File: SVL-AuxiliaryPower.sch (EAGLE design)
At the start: 24 parts

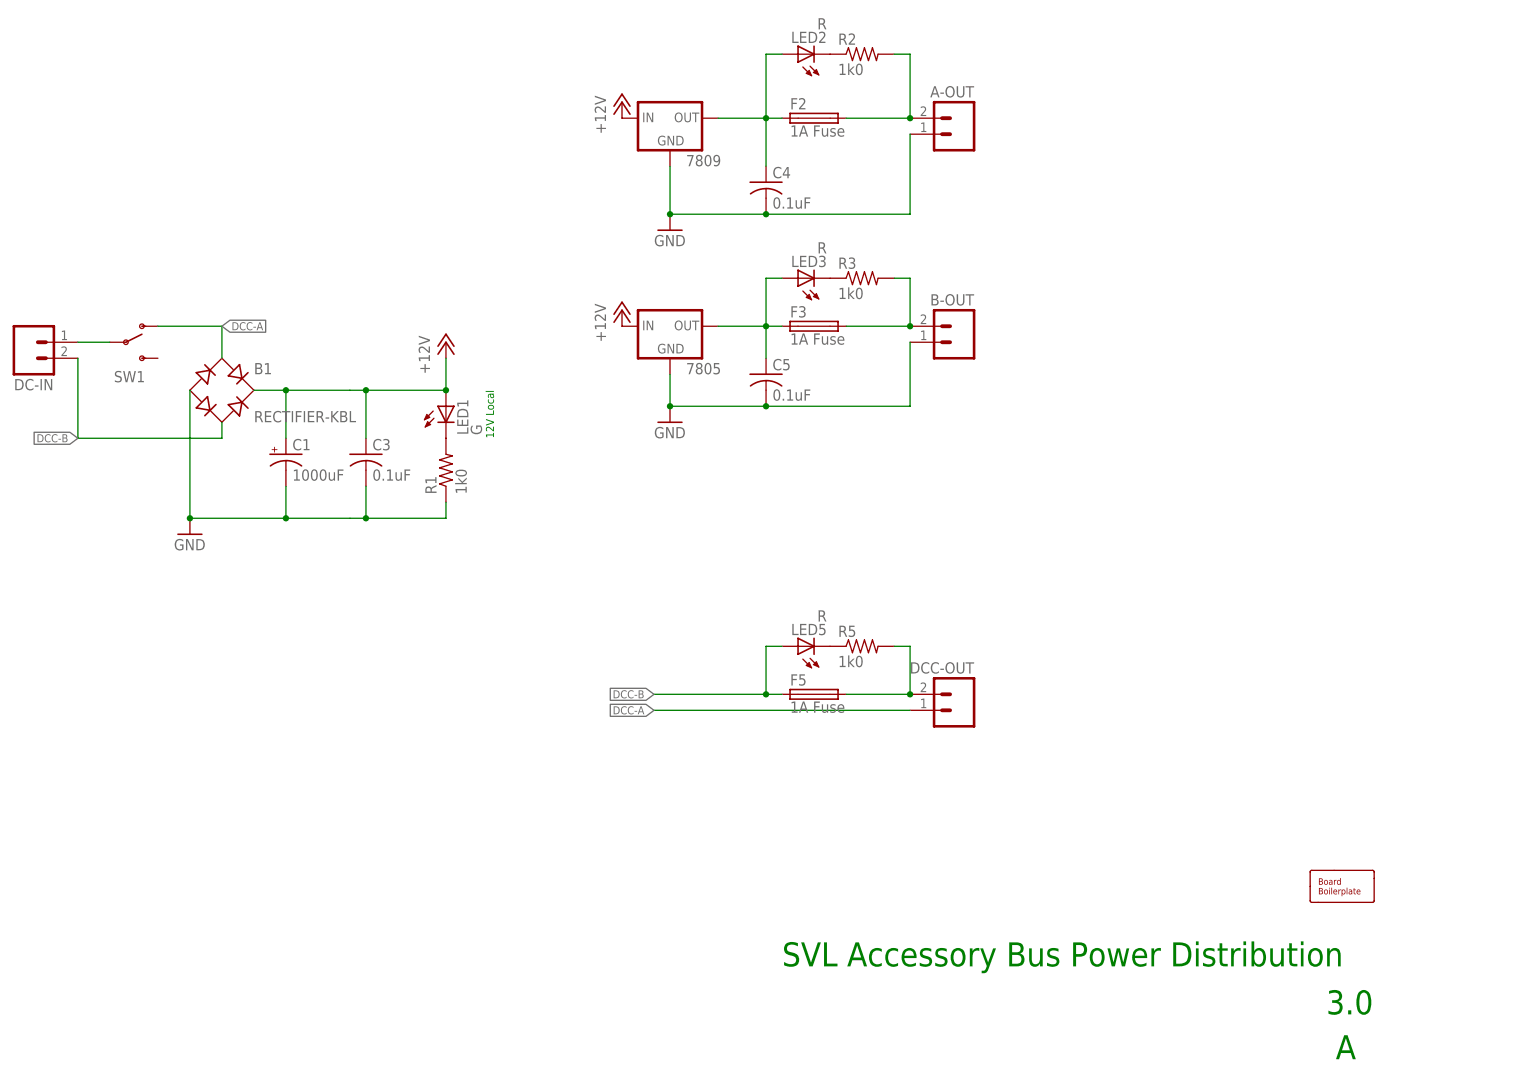
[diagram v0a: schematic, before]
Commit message: normalized values
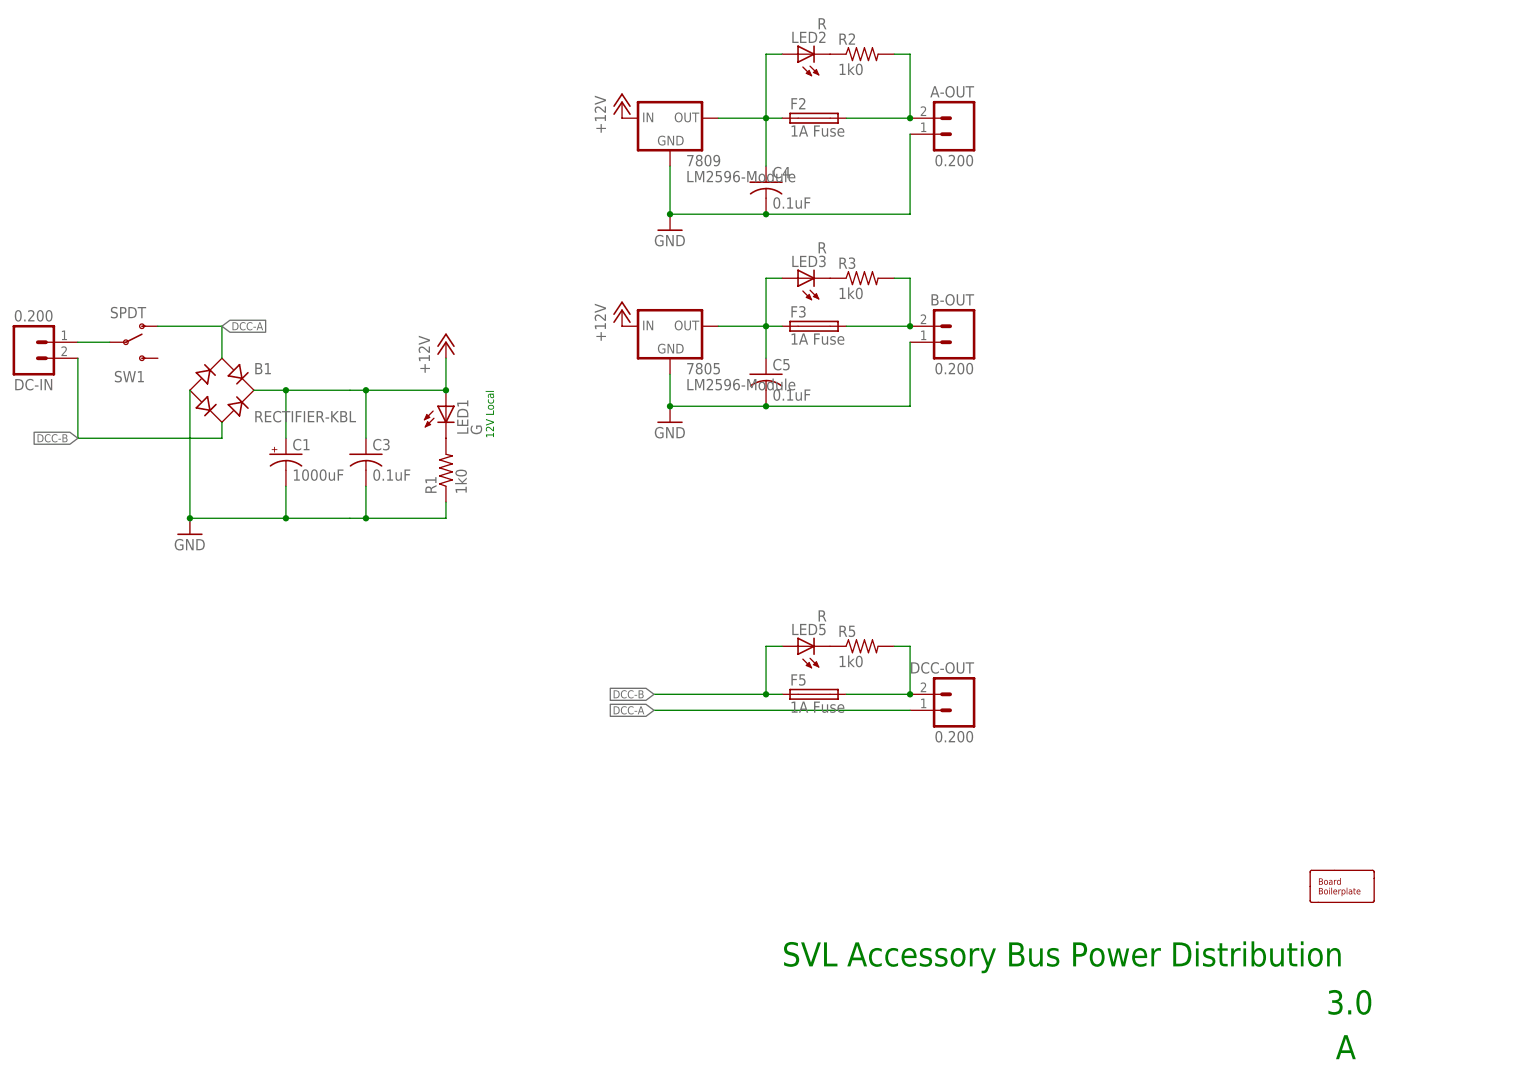
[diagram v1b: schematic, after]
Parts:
- 7805, 7809: value (none) -> LM2596-Module
- A-OUT, B-OUT, DC-IN, DCC-OUT: value (none) -> 0.200
- SW1: value (none) -> SPDT
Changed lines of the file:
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@@
 <parts>
 <part name="FRAME1" library="SPCoast" deviceset="DOC-FRAME-LETTER" device=""/>
-<part name="DCC-OUT" library="SPCoast" deviceset="CONNECTOR-M02" device="508-LOCK"/>
-<part name="B-OUT" library="SPCoast" deviceset="CONNECTOR-M02" device="508-LOCK"/>
+<part name="DCC-OUT" library="SPCoast" deviceset="CONNECTOR-M02" device="508-LOCK" value="0.200"/>
+<part name="B-OUT" library="SPCoast" deviceset="CONNECTOR-M02" device="508-LOCK" value="0.200"/>
 <part name="BOARD1" library="SPCoast" deviceset="BOARD" device="100X100"/>
-<part name="7809" library="SPCoast" deviceset="VREG_78XX" device="LM2596"/>
-<part name="7805" library="SPCoast" deviceset="VREG_78XX" device="LM2596"/>
+<part name="7809" library="SPCoast" deviceset="VREG_78XX" device="LM2596" value="LM2596-Module"/>
+<part name="7805" library="SPCoast" deviceset="VREG_78XX" device="LM2596" value="LM2596-Module"/>
 <part name="B1" library="rectifier" deviceset="RECTIFIER-" device="KBL" value="RECTIFIER-KBL"/>
 <part name="GND1" library="supply1" deviceset="GND" device=""/>
 <part name="GND2" library="supply1" deviceset="GND" device=""/>
 <part name="GND3" library="supply1" deviceset="GND" device=""/>
-<part name="SW1" library="SPCoast" deviceset="SWITCH-SPST" device="PTH-508"/>
+<part name="SW1" library="SPCoast" deviceset="SWITCH-SPST" device="PTH-508" value="SPDT"/>
 <part name="C1" library="SPCoast" deviceset="CAP-POL*" device="PTH-5MM" value="1000uF"/>
 <part name="C3" library="SPCoast" deviceset="CAP*" device="PTH1" value="0.1uF"/>
@@
 <part name="F2" library="SPCoast" deviceset="PICOFUSE" device="POLY" value="1A Fuse"/>
 <part name="F3" library="SPCoast" deviceset="PICOFUSE" device="POLY" value="1A Fuse"/>
-<part name="DC-IN" library="SPCoast" deviceset="CONNECTOR-M02" device="508-LOCK"/>
+<part name="DC-IN" library="SPCoast" deviceset="CONNECTOR-M02" device="508-LOCK" value="0.200"/>
 <part name="P+2" library="supply1" deviceset="+12V" device=""/>
-<part name="A-OUT" library="SPCoast" deviceset="CONNECTOR-M02" device="508-LOCK"/>
+<part name="A-OUT" library="SPCoast" deviceset="CONNECTOR-M02" device="508-LOCK" value="0.200"/>
 <part name="F5" library="SPCoast" deviceset="PICOFUSE" device="POLY" value="1A Fuse"/>
 <part name="P+4" library="supply1" deviceset="+12V" device=""/>
